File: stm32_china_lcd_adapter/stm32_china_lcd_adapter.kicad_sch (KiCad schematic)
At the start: 18 parts, among them J1 China_40P_LCD, J2 China_40P_LCD, J3 China_6P_CTP, U1 MT9284-28J

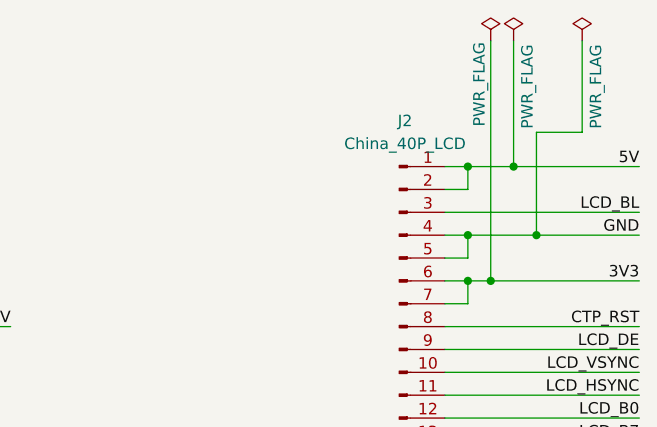
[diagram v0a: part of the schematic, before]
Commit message: adding dumb passive lcd adapter for wildfire and stm32h7 chinese board
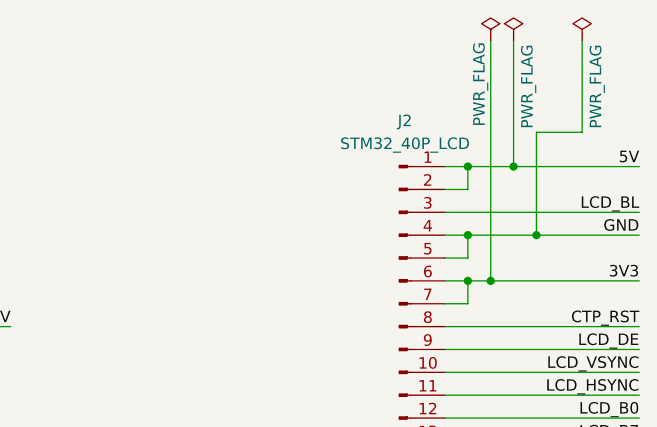
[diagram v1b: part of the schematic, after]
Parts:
- J2: value China_40P_LCD -> STM32_40P_LCD
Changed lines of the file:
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@@
 			)
 		)
-		(property "Value" "China_40P_LCD"
+		(property "Value" "STM32_40P_LCD"
 			(at 240.665 30.48 0)
 			(show_name no)

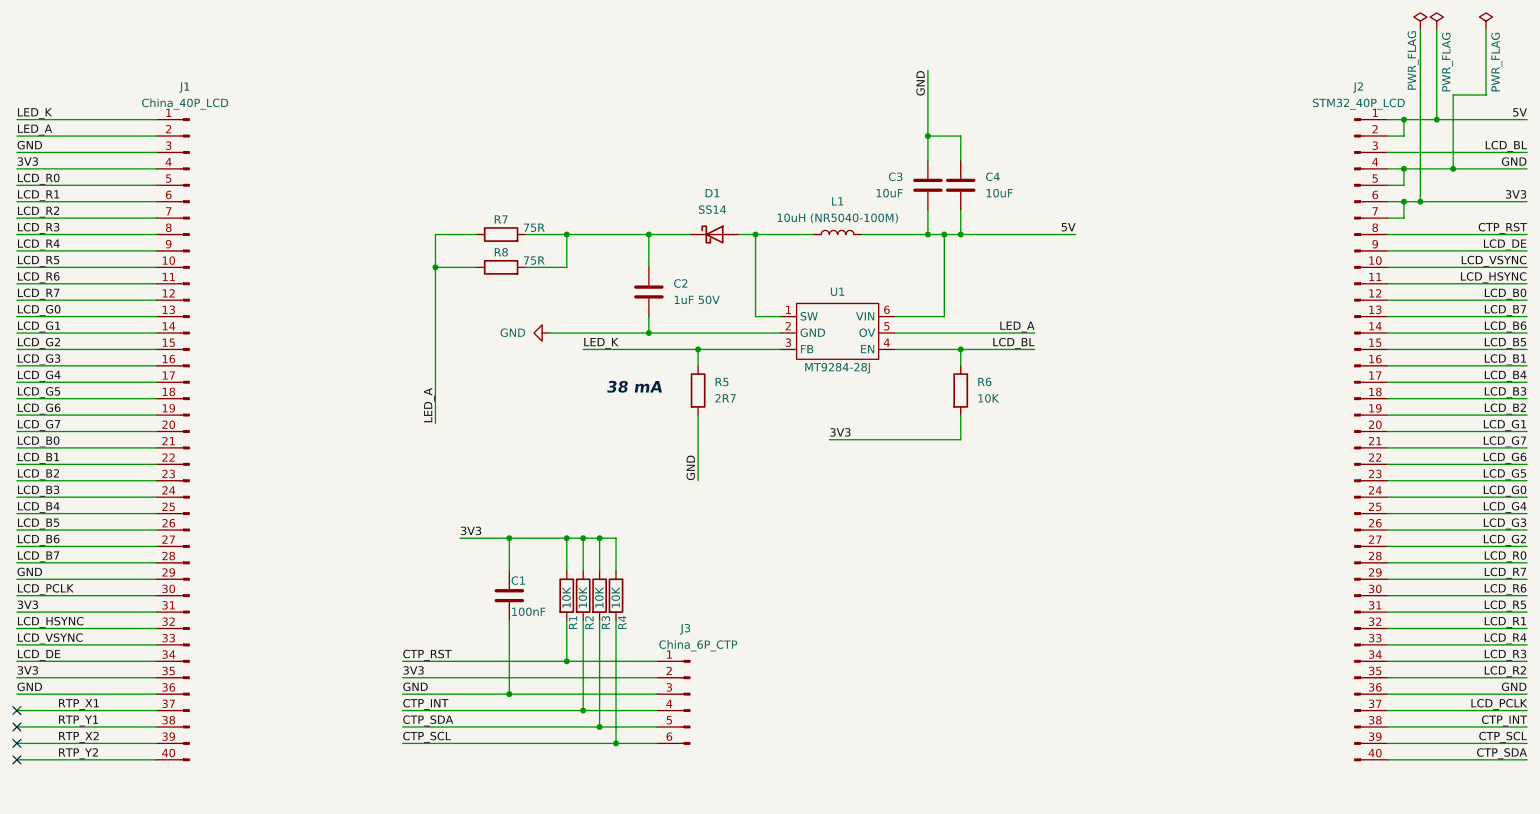
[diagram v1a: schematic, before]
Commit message: upgradinng lcd adapter with blacklight power
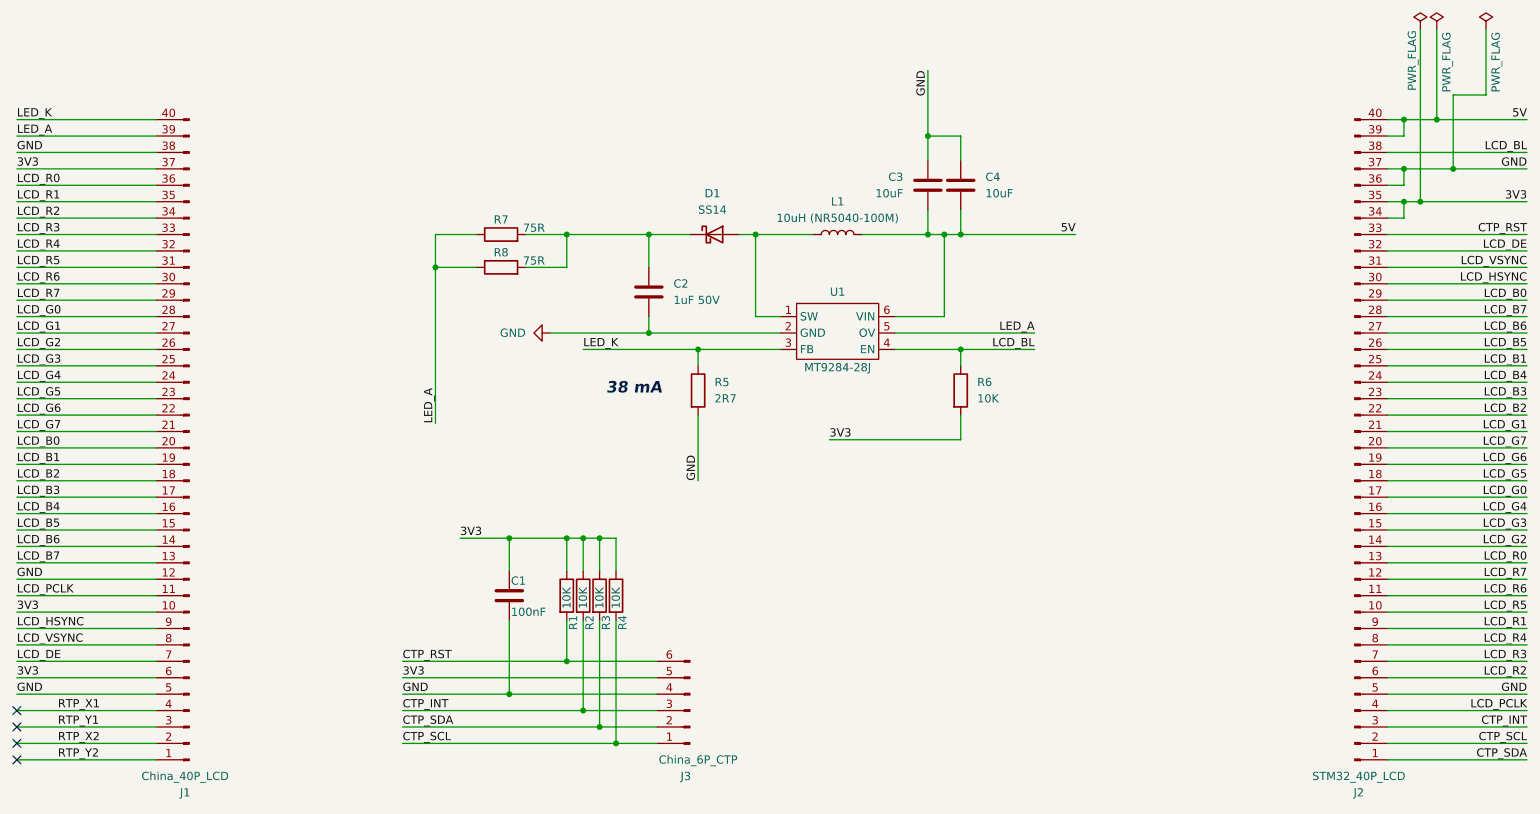
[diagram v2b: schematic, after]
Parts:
- J1, J2: footprint Connector_FFC-FPC:Hirose_FH12-40S-0.5SH_1x40-1MP_P0.50mm_Horizontal -> Connector_FFC-FPC:TE_4-1734839-0_1x40-1MP_P0.5mm_Horizontal
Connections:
- net 3V3: now also J1.10 (Pin_10), J1.37 (Pin_37), J1.6 (Pin_6), J2.34 (Pin_34), J2.35 (Pin_35), J3.5 (Pin_5); no longer J1.31 (Pin_31), J1.35 (Pin_35), J1.4 (Pin_4), J2.6 (Pin_6), J2.7 (Pin_7), J3.2 (Pin_2)
- net 5V: now also J2.39 (Pin_39), J2.40 (Pin_40); no longer J2.1 (Pin_1), J2.2 (Pin_2)
- net CTP_INT: now also J2.3 (Pin_3), J3.3 (Pin_3); no longer J2.38 (Pin_38), J3.4 (Pin_4)
- net CTP_RST: now also J2.33 (Pin_33), J3.6 (Pin_6); no longer J2.8 (Pin_8), J3.1 (Pin_1)
- net CTP_SCL: now also J2.2 (Pin_2), J3.1 (Pin_1); no longer J2.39 (Pin_39), J3.6 (Pin_6)
- net CTP_SDA: now also J2.1 (Pin_1), J3.2 (Pin_2); no longer J2.40 (Pin_40), J3.5 (Pin_5)
- net GND: now also J1.12 (Pin_12), J1.38 (Pin_38), J1.5 (Pin_5), J2.37 (Pin_37), J3.4 (Pin_4); no longer J1.29 (Pin_29), J1.3 (Pin_3), J1.36 (Pin_36), J2.4 (Pin_4), J3.3 (Pin_3)
- net LCD_B0: now also J1.20 (Pin_20), J2.29 (Pin_29); no longer J1.21 (Pin_21), J2.12 (Pin_12)
- net LCD_B1: now also J1.19 (Pin_19), J2.25 (Pin_25); no longer J1.22 (Pin_22), J2.16 (Pin_16)
- net LCD_B2: now also J1.18 (Pin_18), J2.22 (Pin_22); no longer J1.23 (Pin_23), J2.19 (Pin_19)
- net LCD_B3: now also J1.17 (Pin_17), J2.23 (Pin_23); no longer J1.24 (Pin_24), J2.18 (Pin_18)
- net LCD_B4: now also J1.16 (Pin_16), J2.24 (Pin_24); no longer J1.25 (Pin_25), J2.17 (Pin_17)
- net LCD_B5: now also J1.15 (Pin_15), J2.26 (Pin_26); no longer J1.26 (Pin_26), J2.15 (Pin_15)
- net LCD_B6: now also J1.14 (Pin_14), J2.27 (Pin_27); no longer J1.27 (Pin_27), J2.14 (Pin_14)
- net LCD_B7: now also J1.13 (Pin_13), J2.28 (Pin_28); no longer J1.28 (Pin_28), J2.13 (Pin_13)
- net LCD_BL: now also J2.38 (Pin_38); no longer J2.3 (Pin_3)
- net LCD_DE: now also J1.7 (Pin_7), J2.32 (Pin_32); no longer J1.34 (Pin_34), J2.9 (Pin_9)
- net LCD_G0: now also J1.28 (Pin_28), J2.17 (Pin_17); no longer J1.13 (Pin_13), J2.24 (Pin_24)
- net LCD_G1: now also J1.27 (Pin_27), J2.21 (Pin_21); no longer J1.14 (Pin_14), J2.20 (Pin_20)
- net LCD_G2: now also J1.26 (Pin_26), J2.14 (Pin_14); no longer J1.15 (Pin_15), J2.27 (Pin_27)
- net LCD_G3: now also J1.25 (Pin_25), J2.15 (Pin_15); no longer J1.16 (Pin_16), J2.26 (Pin_26)
- net LCD_G4: now also J1.24 (Pin_24), J2.16 (Pin_16); no longer J1.17 (Pin_17), J2.25 (Pin_25)
- net LCD_G5: now also J1.23 (Pin_23), J2.18 (Pin_18); no longer J1.18 (Pin_18), J2.23 (Pin_23)
- net LCD_G6: now also J1.22 (Pin_22), J2.19 (Pin_19); no longer J1.19 (Pin_19), J2.22 (Pin_22)
- net LCD_G7: now also J1.21 (Pin_21), J2.20 (Pin_20); no longer J1.20 (Pin_20), J2.21 (Pin_21)
- net LCD_HSYNC: now also J1.9 (Pin_9), J2.30 (Pin_30); no longer J1.32 (Pin_32), J2.11 (Pin_11)
- net LCD_PCLK: now also J1.11 (Pin_11), J2.4 (Pin_4); no longer J1.30 (Pin_30), J2.37 (Pin_37)
- net LCD_R0: now also J1.36 (Pin_36), J2.13 (Pin_13); no longer J1.5 (Pin_5), J2.28 (Pin_28)
- net LCD_R1: now also J1.35 (Pin_35), J2.9 (Pin_9); no longer J1.6 (Pin_6), J2.32 (Pin_32)
- net LCD_R2: now also J1.34 (Pin_34), J2.6 (Pin_6); no longer J1.7 (Pin_7), J2.35 (Pin_35)
- net LCD_R3: now also J1.33 (Pin_33), J2.7 (Pin_7); no longer J1.8 (Pin_8), J2.34 (Pin_34)
- net LCD_R4: now also J1.32 (Pin_32), J2.8 (Pin_8); no longer J1.9 (Pin_9), J2.33 (Pin_33)
- net LCD_R5: now also J1.31 (Pin_31), J2.10 (Pin_10); no longer J1.10 (Pin_10), J2.31 (Pin_31)
- net LCD_R6: now also J1.30 (Pin_30), J2.11 (Pin_11); no longer J1.11 (Pin_11), J2.30 (Pin_30)
- net LCD_R7: now also J1.29 (Pin_29), J2.12 (Pin_12); no longer J1.12 (Pin_12), J2.29 (Pin_29)
- net LCD_VSYNC: now also J1.8 (Pin_8), J2.31 (Pin_31); no longer J1.33 (Pin_33), J2.10 (Pin_10)
- net LED_A: now also J1.39 (Pin_39); no longer J1.2 (Pin_2)
- net LED_K: now also J1.40 (Pin_40); no longer J1.1 (Pin_1)
- net RTP_X1: now also J1.4 (Pin_4); no longer J1.37 (Pin_37)
- net RTP_X2: now also J1.2 (Pin_2); no longer J1.39 (Pin_39)
- net RTP_Y1: now also J1.3 (Pin_3); no longer J1.38 (Pin_38)
- net RTP_Y2: now also J1.1 (Pin_1); no longer J1.40 (Pin_40)
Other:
- moved on the sheet: J1, J3
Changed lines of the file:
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@@
 	(title_block
 		(title "MBS China STM32 LCD")
-		(date "2026-05-06")
-		(rev "0.1")
+		(date "2026-06-06")
+		(rev "0.2")
 		(company "MBS CLass@")
 	)
@@
 	(symbol
 		(lib_id "Connector:Conn_01x40_Pin")
-		(at 240.03 81.28 0)
+		(at 240.03 83.82 0)
+		(mirror x)
 		(unit 1)
 		(body_style 1)
@@
 		(dnp no)
 		(property "Reference" "J2"
-			(at 240.665 27.94 0)
+			(at 240.665 137.16 0)
 			(show_name no)
 			(do_not_autoplace no)
@@
 		)
 		(property "Value" "STM32_40P_LCD"
-			(at 240.665 30.48 0)
+			(at 240.665 134.62 0)
 			(show_name no)
 			(do_not_autoplace no)
@@
 			)
 		)
-		(property "Footprint" "Connector_FFC-FPC:Hirose_FH12-40S-0.5SH_1x40-1MP_P0.50mm_Horizontal"
-			(at 240.03 81.28 0)
+		(property "Footprint" "Connector_FFC-FPC:TE_4-1734839-0_1x40-1MP_P0.5mm_Horizontal"
+			(at 240.03 83.82 0)
 			(hide yes)
 			(show_name no)
@@
 		)
 		(property "Datasheet" ""
-			(at 240.03 81.28 0)
+			(at 240.03 83.82 0)
 			(hide yes)
 			(show_name no)
@@
 		)
 		(property "Description" "Generic connector, single row, 01x40, script generated"
-			(at 240.03 81.28 0)
+			(at 240.03 83.82 0)
 			(hide yes)
 			(show_name no)
@@
 	(symbol
 		(lib_id "Connector:Conn_01x06_Pin")
-		(at 137.16 121.92 0)
-		(mirror y)
+		(at 137.16 124.46 180)
 		(unit 1)
 		(body_style 1)
@@
 		(dnp no)
 		(property "Reference" "J3"
-			(at 136.525 111.76 0)
+			(at 136.525 134.62 0)
 			(show_name no)
 			(do_not_autoplace no)
@@
 		)
 		(property "Value" "China_6P_CTP"
-			(at 138.4366 114.3 0)
+			(at 138.4366 132.08 0)
 			(show_name no)
 			(do_not_autoplace no)
@@
 		)
 		(property "Footprint" "Connector_FFC-FPC:Hirose_FH12-6S-0.5SH_1x06-1MP_P0.50mm_Horizontal"
-			(at 137.16 121.92 0)
+			(at 137.16 124.46 0)
 			(hide yes)
 			(show_name no)
@@
 		)
 		(property "Datasheet" ""
-			(at 137.16 121.92 0)
+			(at 137.16 124.46 0)
 			(hide yes)
 			(show_name no)
@@
 		)
 		(property "Description" "Generic connector, single row, 01x06, script generated"
-			(at 137.16 121.92 0)
+			(at 137.16 124.46 0)
 			(hide yes)
 			(show_name no)
@@
 	(symbol
 		(lib_id "Connector:Conn_01x40_Pin")
-		(at 59.69 81.28 0)
-		(mirror y)
+		(at 59.69 83.82 180)
 		(unit 1)
 		(body_style 1)
@@
 		(dnp no)
 		(property "Reference" "J1"
-			(at 59.055 27.94 0)
+			(at 59.055 137.16 0)
 			(show_name no)
 			(do_not_autoplace no)
@@
 		)
 		(property "Value" "China_40P_LCD"
-			(at 59.055 30.48 0)
+			(at 59.055 134.62 0)
 			(show_name no)
 			(do_not_autoplace no)
@@
 			)
 		)
-		(property "Footprint" "Connector_FFC-FPC:Hirose_FH12-40S-0.5SH_1x40-1MP_P0.50mm_Horizontal"
-			(at 59.69 81.28 0)
+		(property "Footprint" "Connector_FFC-FPC:TE_4-1734839-0_1x40-1MP_P0.5mm_Horizontal"
+			(at 59.69 83.82 0)
 			(hide yes)
 			(show_name no)
@@
 		)
 		(property "Datasheet" ""
-			(at 59.69 81.28 0)
+			(at 59.69 83.82 0)
 			(hide yes)
 			(show_name no)
@@
 		)
 		(property "Description" "Generic connector, single row, 01x40, script generated"
-			(at 59.69 81.28 0)
+			(at 59.69 83.82 0)
 			(hide yes)
 			(show_name no)
